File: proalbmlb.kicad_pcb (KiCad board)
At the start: 4 copper layers, 71 x 76.3 mm, 42 parts, among them J1 DE9_Pins_MountingHoles, J10 Conn_01x08_Socket, J2 Conn_01x08_Socket, J3 HPF-02-01-X-S, J4 Conn_01x04_Socket, J6 Conn_01x04_Socket, J8 Conn_01x02_Pin, U10 PTMUX6236RUMR, U11 TMUX7219MDGKR, U12 PTMUX6236RUMR, U3 TMUX7201RQXR, U7 PINA745AIRELR, U8 PTMUX6236RUMR, U9 PINA745AIRELR

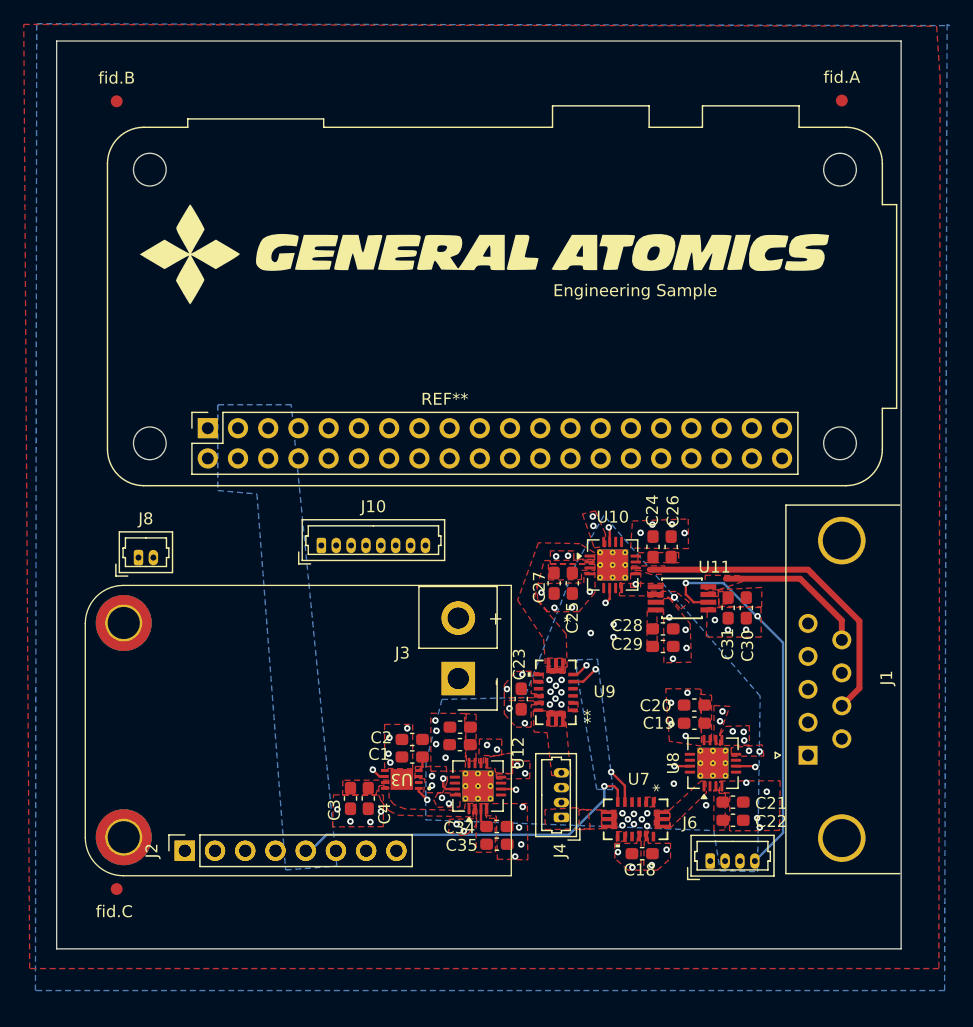
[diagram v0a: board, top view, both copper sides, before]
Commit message: remove blind/buried vias. trim demensions, add mounting holes, fix nets
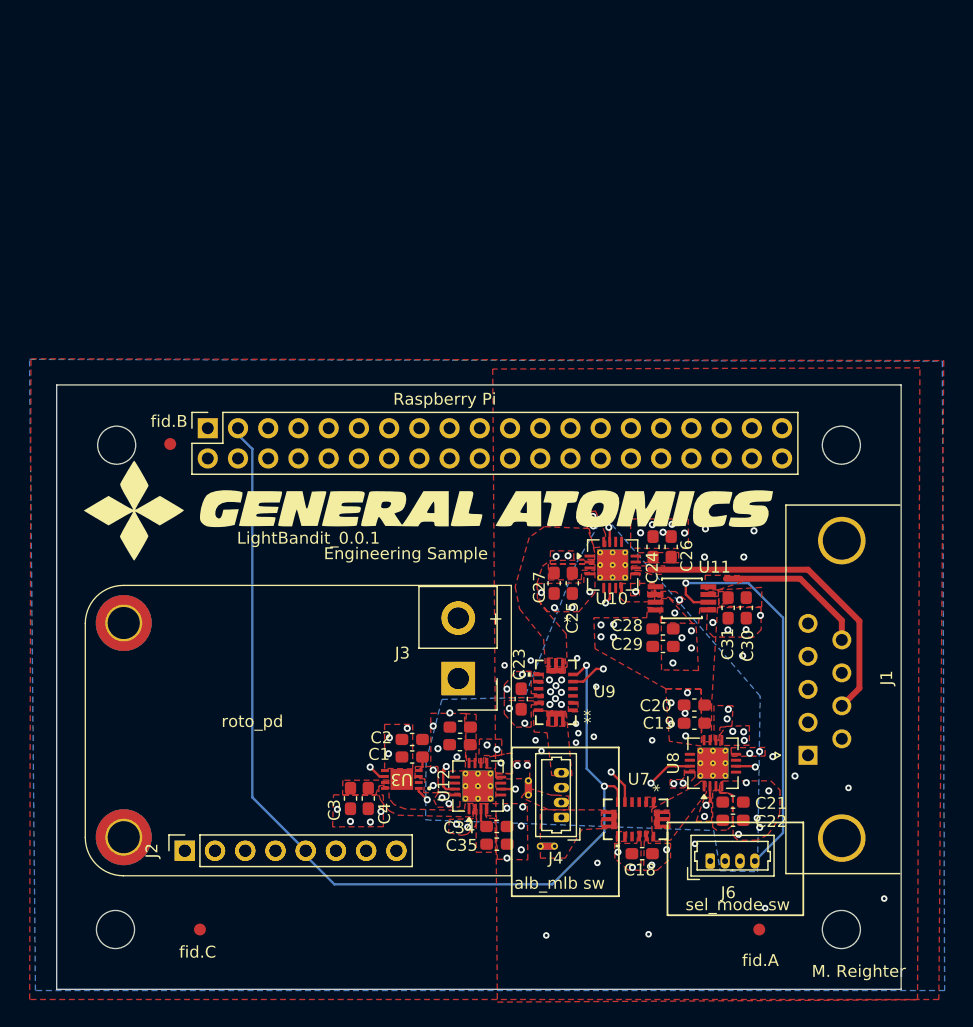
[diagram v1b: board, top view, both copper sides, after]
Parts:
- removed J10: Conn_01x08_Socket, Connector_Molex:Molex_PicoBlade_53047-0810_1x08_P1.25mm_Vertical
- removed J8: Conn_01x02_Pin, Connector_Molex:Molex_PicoBlade_53047-0210_1x02_P1.25mm_Vertical
- added REF**: NetTie-2_THT_Pad0.3mm, NetTie:NetTie-2_THT_Pad0.3mm, F.Cu at (151.1, 104.1)
- added REF**: MountingHole_3.2mm_M3_ISO7380, MountingHole:MountingHole_3.2mm_M3_ISO7380, F.Cu at (116.5, 75.9)
- added REF**: MountingHole_3.2mm_M3_ISO7380, MountingHole:MountingHole_3.2mm_M3_ISO7380, F.Cu at (116.4, 116.6)
- added REF**: MountingHole_3.2mm_M3_ISO7380, MountingHole:MountingHole_3.2mm_M3_ISO7380, F.Cu at (177.4, 75.9)
- added REF**: MountingHole_3.2mm_M3_ISO7380, MountingHole:MountingHole_3.2mm_M3_ISO7380, F.Cu at (177.4, 116.6)
- added REF**: NetTie-2_THT_Pad0.3mm, NetTie:NetTie-2_THT_Pad0.3mm, F.Cu at (152.1, 109.6)
- Raspberry Pi: renamed from REF**
- moved fid.A 70.0 mm to (170.5, 116.6)
- moved fid.B 29.1 mm to (121.0, 75.8)
- moved G*** 22.0 mm to (142.6, 81.4)
- moved fid.C 7.78 mm to (123.5, 116.6)
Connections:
- Raspberry Pi pad 1: (no net) -> +3.3V
- Raspberry Pi pad 14: (no net) -> GND
- Raspberry Pi pad 17: (no net) -> +3.3V
- Raspberry Pi pad 2: (no net) -> +5V
- Raspberry Pi pad 20: (no net) -> GND
- Raspberry Pi pad 25: (no net) -> GND
- Raspberry Pi pad 30: (no net) -> GND
- Raspberry Pi pad 33: (no net) -> /Project Architecture/Raspberrypi/PWM
- Raspberry Pi pad 34: (no net) -> GND
- Raspberry Pi pad 39: (no net) -> GND
- Raspberry Pi pad 4: (no net) -> +5V
- Raspberry Pi pad 6: (no net) -> GND
- Raspberry Pi pad 9: (no net) -> GND
- U7 pad 13: VDD -> /Project Architecture/Motor A/+M
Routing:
- net /Project Architecture/Connectors/SDC: track 32.3 -> 83.3 mm
- net /Project Architecture/Connectors/SDA: track 40.0 -> 85.8 mm
- net /Project Architecture/Raspberrypi/PWM: track 30.0 -> 46.0 mm
- net /Project Architecture/Connectors/+M: track 0.00 -> 7.26 mm
- net /Project Architecture/Connectors/Stow: track 8.74 -> 12.4 mm
- net /Project Architecture/Connectors/J1_1: track 11.2 -> 13.0 mm, vias 1 -> 2
- net /Project Architecture/Connectors/SFF: track 32.7 -> 33.9 mm
- net VDD: track 21.2 -> 20.9 mm, vias 4 -> 5
- net GND: track 0.07 -> 0.00 mm, vias 83 -> 84
- net /Project Architecture/Connectors/J1_2: vias 1 -> 2
- net /Project Architecture/Connectors/J1_8: vias 2 -> 1
- added copper zone on In1.Cu, net /Project Architecture/Connectors/J1_1
- added copper zone on In1.Cu, net /Project Architecture/Connectors/J1_2
- removed copper zone on In2.Cu, net /Project Architecture/Connectors/SDA
- removed copper zone on B.Cu, net /Project Architecture/Connectors/SDC
- removed copper zone on In2.Cu, net /Project Architecture/Raspberrypi/PWM
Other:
- board size 71 x 76.3 mm -> 71 x 50.8 mm
- board text added: "LightBandit_0.0.1"
- board text added: "M. Reighter"
- board text added: "alb_mlb sw"
- board text added: "roto_pd"
- board text added: "sel_mode sw"
- board text removed: "X"
- board text removed: "Y"

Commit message: Update Outputs
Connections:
- C3 pad 2: Net-(U8-VSS) -> VDD
- C4 pad 2: Net-(U8-VSS) -> VDD
- J3 pad 1: GND -> (no net)
- J3 pad 2: VDD -> (no net)
- U1 pad 3: unconnected-(U1-PD_INT_3V-Pad3)_6 -> /Project Architecture/RotoPD/unconnected-(U1-PD_INT_3V-Pad3)_6
- U1 pad 5: /Project Architecture/Connectors/SDC -> /Project Architecture/Connectors/SDA
- U12 pad : GND -> (no net)
- U3 pad 7: Net-(U8-VSS) -> VDD
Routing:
- net /Project Architecture/Connectors/J1_4: track 0.00 -> 8.59 mm
- net /Project Architecture/Connectors/J1_3: track 0.00 -> 7.19 mm, vias 2 -> 0
- net /Project Architecture/Connectors/J1_5: track 24.9 -> 27.9 mm
- net /Project Architecture/Connectors/+M: track 7.26 -> 7.96 mm
- net GND: vias 84 -> 92
- removed copper zone on In1.Cu, net /Project Architecture/Connectors/J1_3
